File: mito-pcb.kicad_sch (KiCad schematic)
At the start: 6 parts

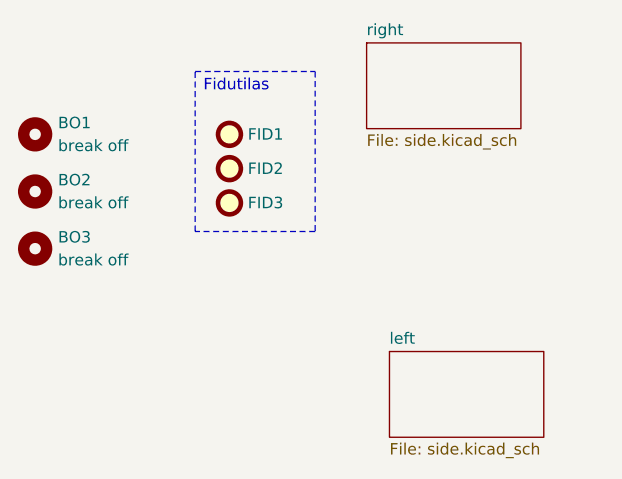
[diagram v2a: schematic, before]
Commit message: made progress, added xiao libray, removed almost all of the old schmeatic, started ot edit pcb
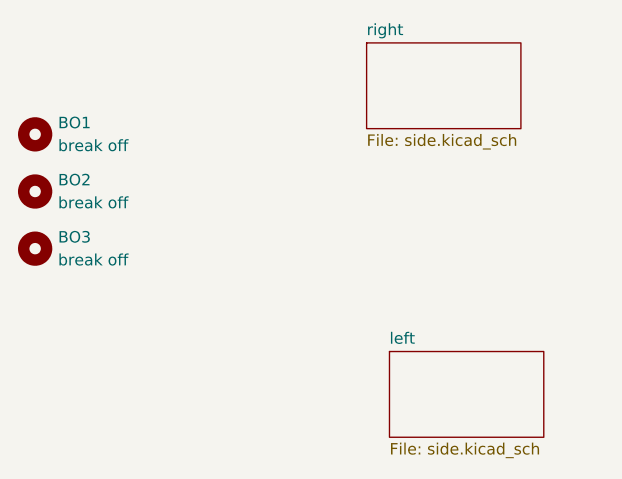
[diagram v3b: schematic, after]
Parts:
- removed FID1, FID2, FID3: Fiducial, Fiducial:Fiducial_1.5mm_Mask3mm, symbol Mechanical:Fiducial
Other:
- note removed: "Fidutilas"
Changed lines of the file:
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@@
 	(generator_version "9.0")
 	(paper "A4")
-	(rectangle
-		(start 107.95 103.505)
-		(end 121.285 121.285)
-		(stroke
-			(width 0)
-			(type dash)
-		)
-		(fill
-			(type none)
-		)
-	)
-	(text "Fidutilas\n\n"
-		(exclude_from_sim no)
-		(at 112.522 106.172 0)
-		(effects
-			(font
-				(size 1.27 1.27)
-			)
-		)
-	)
 	(symbol
 		(lib_id "Mechanical:MountingHole")
@@
 				(path "/2b736a6b-c6e2-42fa-94c9-e384d663659b"
 					(reference "BO3")
-					(unit 1)
-				)
-			)
-		)
-	)
-	(symbol
-		(lib_id "Mechanical:Fiducial")
-		(at 111.76 114.3 0)
-		(unit 1)
-		(exclude_from_sim yes)
-		(in_bom no)
-		(on_board yes)
-		(dnp no)
-		(property "Reference" "FID2"
-			(at 113.792 114.3 0)
-			(effects
-				(font
-					(size 1.27 1.27)
-				)
-				(justify left)
-			)
-		)
-		(property "Value" "Fiducial"
-			(at 114.3 115.5699 0)
-			(effects
-				(font
-					(size 1.27 1.27)
-				)
-				(justify left)
-				(hide yes)
-			)
-		)
-		(property "Footprint" "Fiducial:Fiducial_1.5mm_Mask3mm"
-			(at 111.76 114.3 0)
-			(effects
-				(font
-					(size 1.27 1.27)
-				)
-				(hide yes)
-			)
-		)
-		(property "Datasheet" "~"
-			(at 111.76 114.3 0)
-			(effects
-				(font
-					(size 1.27 1.27)
-				)
-				(hide yes)
-			)
-		)
-		(property "Description" "Fiducial Marker"
-			(at 111.76 114.3 0)
-			(effects
-				(font
-					(size 1.27 1.27)
-				)
-				(hide yes)
-			)
-		)
-		(instances
-			(project "koeg-board-pcb"
-				(path "/2b736a6b-c6e2-42fa-94c9-e384d663659b"
-					(reference "FID2")
-					(unit 1)
-				)
-			)
-		)
-	)
-	(symbol
-		(lib_id "Mechanical:Fiducial")
-		(at 111.76 110.49 0)
-		(unit 1)
-		(exclude_from_sim yes)
-		(in_bom no)
-		(on_board yes)
-		(dnp no)
-		(property "Reference" "FID1"
-			(at 113.792 110.49 0)
-			(effects
-				(font
-					(size 1.27 1.27)
-				)
-				(justify left)
-			)
-		)
-		(property "Value" "Fiducial"
-			(at 114.3 111.7599 0)
-			(effects
-				(font
-					(size 1.27 1.27)
-				)
-				(justify left)
-				(hide yes)
-			)
-		)
-		(property "Footprint" "Fiducial:Fiducial_1.5mm_Mask3mm"
-			(at 111.76 110.49 0)
-			(effects
-				(font
-					(size 1.27 1.27)
-				)
-				(hide yes)
-			)
-		)
-		(property "Datasheet" "~"
-			(at 111.76 110.49 0)
-			(effects
-				(font
-					(size 1.27 1.27)
-				)
-				(hide yes)
-			)
-		)
-		(property "Description" "Fiducial Marker"
-			(at 111.76 110.49 0)
-			(effects
-				(font
-					(size 1.27 1.27)
-				)
-				(hide yes)
-			)
-		)
-		(instances
-			(project "koeg-board-pcb"
-				(path "/2b736a6b-c6e2-42fa-94c9-e384d663659b"
-					(reference "FID1")
 					(unit 1)
 				)
@@
 					(unit 1)
 				)
-			)
-		)
-	)
-	(symbol
-		(lib_id "Mechanical:Fiducial")
-		(at 111.76 118.11 0)
-		(unit 1)
-		(exclude_from_sim yes)
-		(in_bom no)
-		(on_board yes)
-		(dnp no)
-		(property "Reference" "FID3"
-			(at 113.792 118.11 0)
-			(effects
-				(font
-					(size 1.27 1.27)
-				)
-				(justify left)
-			)
-		)
-		(property "Value" "Fiducial"
-			(at 114.3 119.3799 0)
-			(effects
-				(font
-					(size 1.27 1.27)
-				)
-				(justify left)
-				(hide yes)
-			)
-		)
-		(property "Footprint" "Fiducial:Fiducial_1.5mm_Mask3mm"
-			(at 111.76 118.11 0)
-			(effects
-				(font
-					(size 1.27 1.27)
-				)
-				(hide yes)
-			)
-		)
-		(property "Datasheet" "~"
-			(at 111.76 118.11 0)
-			(effects
-				(font
-					(size 1.27 1.27)
-				)
-				(hide yes)
-			)
-		)
-		(property "Description" "Fiducial Marker"
-			(at 111.76 118.11 0)
-			(effects
-				(font
-					(size 1.27 1.27)
-				)
-				(hide yes)
-			)
-		)
-		(instances
-			(project "koeg-board-pcb"
-				(path "/2b736a6b-c6e2-42fa-94c9-e384d663659b"
-					(reference "FID3")
-					(unit 1)
-				)
